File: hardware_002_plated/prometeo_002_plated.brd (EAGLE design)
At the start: 33 x 86 mm, 72 parts, among them IC1 STLQ015_SOT23-5L, IC2 MAX11609, IC3 MAX6520, U1 ESP12EPADS_SMD, X1 1503_02, X2 1503_02, X3 1503_02, X4 MKDSN1,5/2-5,08

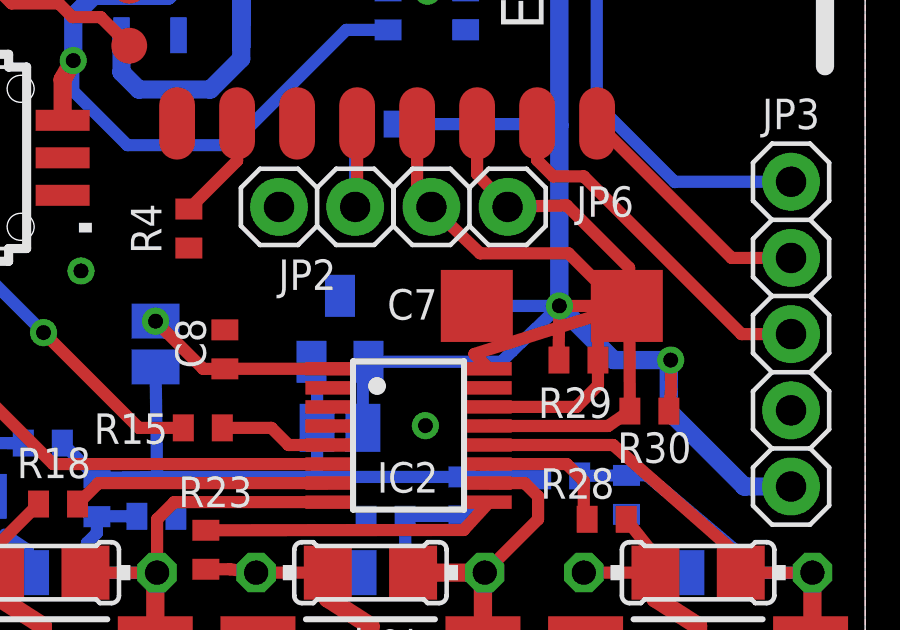
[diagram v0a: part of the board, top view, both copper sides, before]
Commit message: C7 position changed
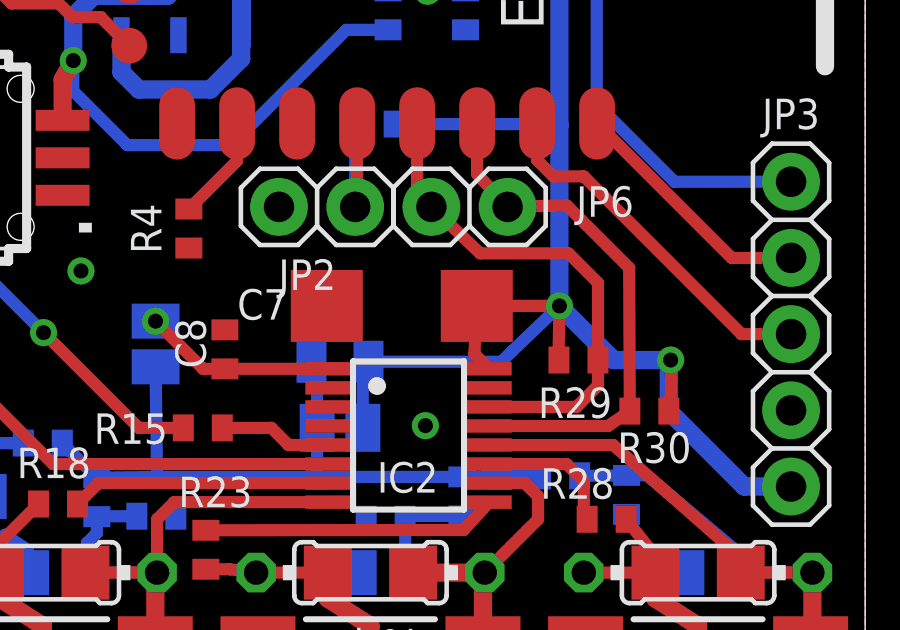
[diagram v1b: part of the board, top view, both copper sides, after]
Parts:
- moved C7 5.00 mm to (17.6, 21.8)
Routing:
- net +3V3: track 93.7 -> 90.4 mm
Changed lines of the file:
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@@
 <attribute name="VALUE" x="20.685" y="19.939" size="1.27" layer="28" rot="MR0"/>
 </element>
-<element name="C7" library="rcl" package="SMC_C" value="100uF" x="22.5552" y="21.844" smashed="yes" rot="R180">
-<attribute name="NAME" x="17.0688" y="21.3868" size="1.016" layer="25"/>
-<attribute name="VALUE" x="24.4602" y="24.384" size="1.016" layer="27" rot="R180"/>
+<element name="C7" library="rcl" package="SMC_C" value="100uF" x="17.5552" y="21.844" smashed="yes" rot="R180">
+<attribute name="NAME" x="12.0688" y="21.3868" size="1.016" layer="25"/>
+<attribute name="VALUE" x="19.4602" y="24.384" size="1.016" layer="27" rot="R180"/>
 </element>
 <element name="SJ1" library="jumper" package="SJ" value="" x="9.3472" y="20.574" smashed="yes" rot="MR270">
@@
 <via x="22.8092" y="21.844" extent="1-16" drill="0.5"/>
 <wire x1="21.24334375" y1="20.34666875" x2="22.8092" y2="21.844" width="0.4064" layer="16"/>
-<wire x1="22.8092" y1="21.844" x2="25.0552" y2="21.844" width="0.4064" layer="1"/>
+<wire x1="22.8092" y1="21.844" x2="20.0552" y2="21.844" width="0.4064" layer="1"/>
 <wire x1="22.7942" y1="20.0406" x2="22.7838" y2="20.432" width="0.4064" layer="1"/>
 <wire x1="22.7838" y1="20.432" x2="22.8092" y2="21.844" width="0.4064" layer="1"/>
@@
 <wire x1="16.444" y1="19.982" x2="20.878675" y2="19.982" width="0.4064" layer="16"/>
 <wire x1="20.878675" y1="19.982" x2="21.24334375" y2="20.34666875" width="0.4064" layer="16"/>
-<wire x1="25.0552" y1="21.844" x2="19.9752" y2="20.2433" width="0.4064" layer="1"/>
+<wire x1="20.0552" y1="21.844" x2="19.9752" y2="20.2433" width="0.4064" layer="1"/>
 <wire x1="19.9752" y1="20.2433" x2="20.47" y2="19.7485" width="0.4064" layer="1"/>
 <wire x1="8.2114" y1="30.8676" x2="8.2114" y2="29.6346" width="0.6096" layer="16"/>
